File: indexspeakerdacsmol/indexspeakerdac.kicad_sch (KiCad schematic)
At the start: 34 parts, among them IC1 MAX98360AEFB+T, IC2 MAX98360AEFB+T, IC3 W25Q16JVUXIQ_TR, J1 Conn_01x04_Pin, J2 Conn_01x04_Pin, U1 RP2040, U2 MIC5317-3.3xM5, Y1 Crystal_GND24

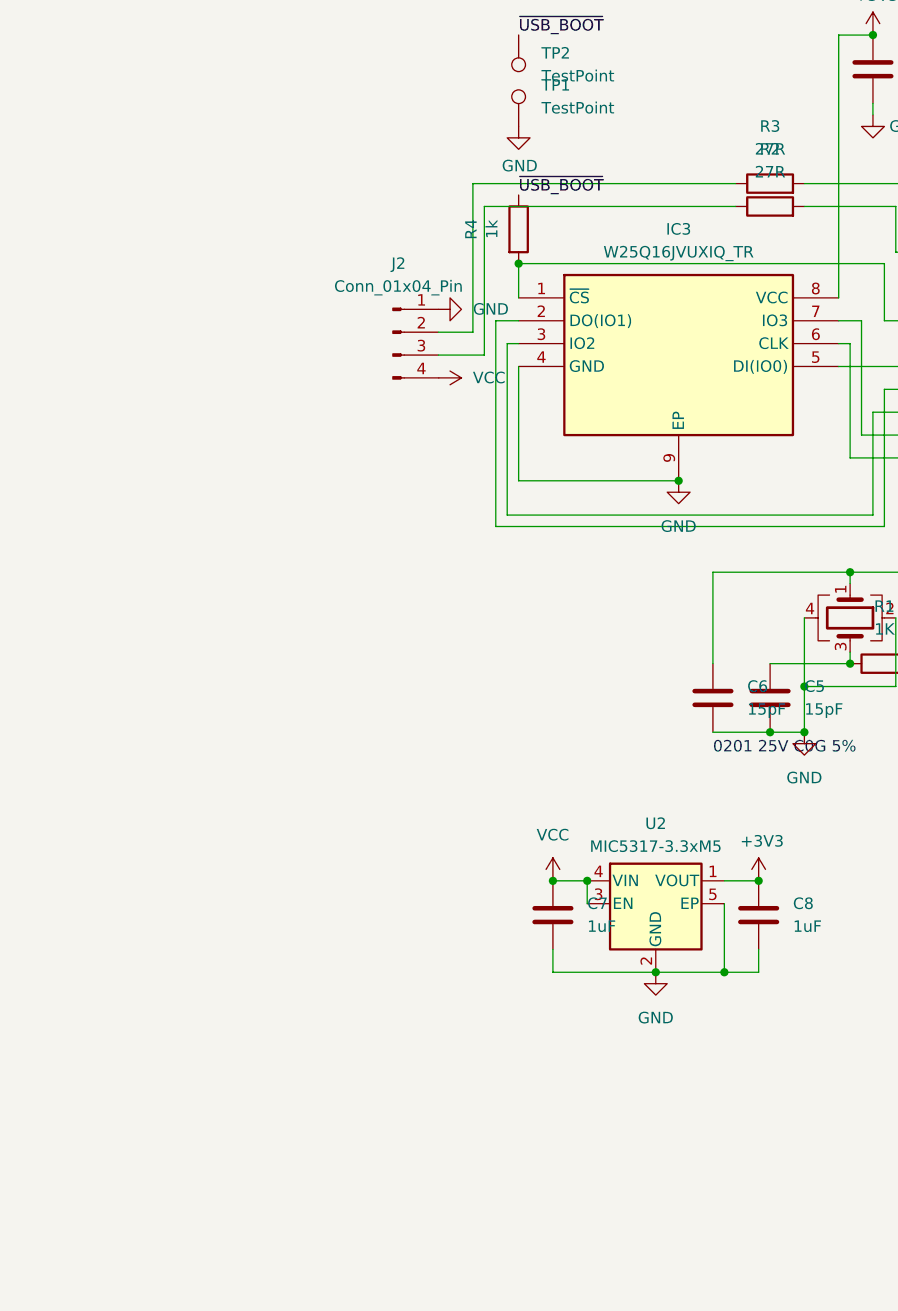
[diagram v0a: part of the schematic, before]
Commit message: add usb c + bom
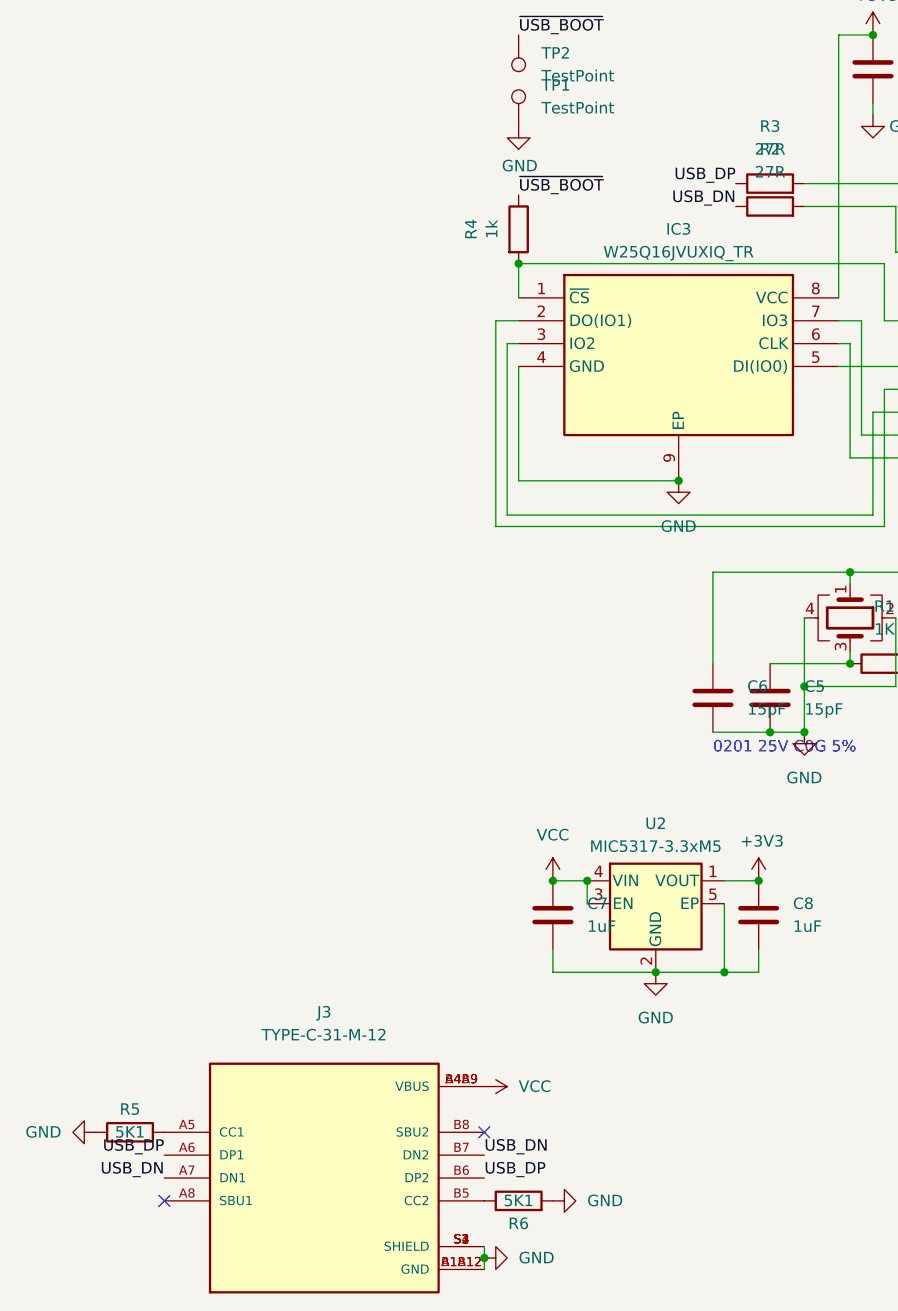
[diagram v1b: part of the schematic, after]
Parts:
- removed J2: Conn_01x04_Pin, Connector_PinHeader_2.00mm:PinHeader_1x04_P2.00mm_Horizontal, symbol Connector:Conn_01x04_Pin
- added J3: TYPE-C-31-M-12, footprint:HRO_TYPE-C-31-M-12, symbol TYPE-C-31-M-12:TYPE-C-31-M-12
- added R5, R6: 5K1, Resistor_SMD:R_0201_0603Metric, symbol Device:R
- IC2: DIGIKEY (none) -> 175-MAX98360AEFB+TDKR-ND
- IC3: LCSC (none) -> C2843335
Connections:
- net GND: now also J3.A1B12 (GND), J3.B1A12 (GND), J3.S1 (SHIELD), J3.S2 (SHIELD), J3.S3 (SHIELD), J3.S4 (SHIELD), R5.1, R6.2
- net VCC: now also J3.A4B9 (VBUS), J3.B4A9 (VBUS)
- net USB_DP: now reaches R3.1
- net USB_DP: now also J3.A6 (DP1), J3.B6 (DP2)
- net USB_DN: now reaches R2.1
- net USB_DN: now also J3.A7 (DN1), J3.B7 (DN2)
- new net: J3.B5 (CC2), R6.1
- new net: J3.A5 (CC1), R5.2
- no-connect marks 29 -> 31
